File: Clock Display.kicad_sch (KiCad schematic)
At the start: 28 parts, among them U11 SA15-11SURKWA, U12 SA15-11SURKWA, U13 SA15-11SURKWA, U14 SA15-11SURKWA, U15 SA15-11SURKWA, U26 SN74LVC244A, U31 SN74LVC244A, U36 SN74LVC244A, U7 SA15-11SURKWA

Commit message: Restructuring
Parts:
- added C27: 1u, Capacitor_SMD:C_0402_1005Metric, symbol Device:C
- added R12, R13: 10R, symbol Device:R
- U11, U12, U13, U14, U15, U7: footprint (none) -> precision_clock:SA15-11SURKWA; Mouser (none) -> 604-SA15-11SURKWA
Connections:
- net GND: now also U31.11 (2A3), U31.13 (2A2), C27.2
- net K7: now also R12.2, R13.1; no longer U26.9 (2Y3)
- net VDIS: now also R13.2
- net DIS7: now reaches U26.11 (2A3)
- net DIS6: now reaches U26.13 (2A2)
- net DIS5: now reaches U26.15 (2A1)
- net DIS4: now reaches U26.17 (2A0)
- net DIS0: now reaches U26.2 (1A0)
- net DIS1: now reaches U26.4 (1A1)
- net DIS2: now reaches U26.6 (1A2)
- net DIS3: now reaches U26.8 (1A3)
- net DIS13: now reaches U31.15 (2A1)
- net DIS12: now reaches U31.17 (2A0)
- net DIS8: now reaches U31.2 (1A0)
- net DIS9: now reaches U31.4 (1A1)
- net DIS10: now reaches U31.6 (1A2)
- net DIS11: now reaches U31.8 (1A3)
- net VC renamed VCOL
- net VCOL: now also C27.1
- new net: R12.1, U26.9 (2Y3)
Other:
- note added: "Current Limiting resistors here needs to be reconsidered"
- note removed: "HHmmSSsss Character matrix drivers"
- moved on the sheet: C25, C26, C44, C45, C47, D16, D17, D18, D19, R45, R46, R47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

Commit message: Removal of Colon LEDs
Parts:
- removed D16, D17, D18, D19: LED, LED_THT:LED_D5.0mm, symbol Device:LED
- added D10, D7, D8, D9: LED, precision_clock:Lite On LTST-C190KxKT, symbol Device:LED
- C37: renamed from C27; footprint Capacitor_SMD:C_0402_1005Metric -> Capacitor_SMD:C_0603_1608Metric
- R16: renamed from R12; footprint (none) -> Resistor_SMD:R_0402_1005Metric
- R17: renamed from R13; footprint (none) -> Resistor_SMD:R_0402_1005Metric
- R28: renamed from R45; footprint Resistor_SMD:R_0603_1608Metric -> Resistor_SMD:R_0402_1005Metric
- R29: renamed from R46; footprint Resistor_SMD:R_0603_1608Metric -> Resistor_SMD:R_0402_1005Metric
- R30: renamed from R47; footprint Resistor_SMD:R_0603_1608Metric -> Resistor_SMD:R_0402_1005Metric
- R31: renamed from R48; footprint Resistor_SMD:R_0603_1608Metric -> Resistor_SMD:R_0402_1005Metric
- R32: renamed from R49; footprint Resistor_SMD:R_0603_1608Metric -> Resistor_SMD:R_0402_1005Metric
- R33: renamed from R50; footprint Resistor_SMD:R_0603_1608Metric -> Resistor_SMD:R_0402_1005Metric
- R34: renamed from R51; footprint Resistor_SMD:R_0603_1608Metric -> Resistor_SMD:R_0402_1005Metric
- R35: renamed from R52; footprint Resistor_SMD:R_0603_1608Metric -> Resistor_SMD:R_0402_1005Metric
- R36: renamed from R53; footprint Resistor_SMD:R_0603_1608Metric -> Resistor_SMD:R_0402_1005Metric
- R37: renamed from R54; footprint Resistor_SMD:R_0603_1608Metric -> Resistor_SMD:R_0402_1005Metric
- renumbered C25 to C27, C44 to C28, C26 to C33, C45 to C34, C47 to C38, U7 to U10, U26 to U11, U11 to U12, U12 to U13, U31 to U14, U13 to U15, U14 to U16, U36 to U17, U15 to U18
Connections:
- net COL0 is gone; now on net LED0: U17.2 (1A0)
- net COL1 is gone; now on net LED1: U17.4 (1A1)
- net COL2 is gone; now on net LED2: U17.6 (1A2)
- net COL3 is gone; now on net LED3: U17.8 (1A3)
- net GND: now also D10.1 (K), D7.1 (K), D8.1 (K), D9.1 (K)
- net LED0: no longer R34.1, U17.18 (1Y0)
- net LED1: no longer R35.1, U17.16 (1Y1)
- net LED2: no longer R36.1, U17.14 (1Y2)
- net LED3: no longer R37.1, U17.12 (1Y3)
- net at R37.2: now also D10.2 (A)
- net at R36.2: now also D9.2 (A)
- net at R35.2: now also D8.2 (A)
- net at R34.2: now also D7.2 (A)
- net VCOL renamed +3.3V
- new net: R35.1, U17.16 (1Y1)
- new net: R37.1, U17.12 (1Y3)
- new net: R36.1, U17.14 (1Y2)
- new net: R34.1, U17.18 (1Y0)
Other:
- note removed: "HH:mm separator"
- note removed: "mm:SS separator"
- moved on the sheet: C27, C28, C33, C34, C37, C38, R16, R17, R28, R29, R30, R31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

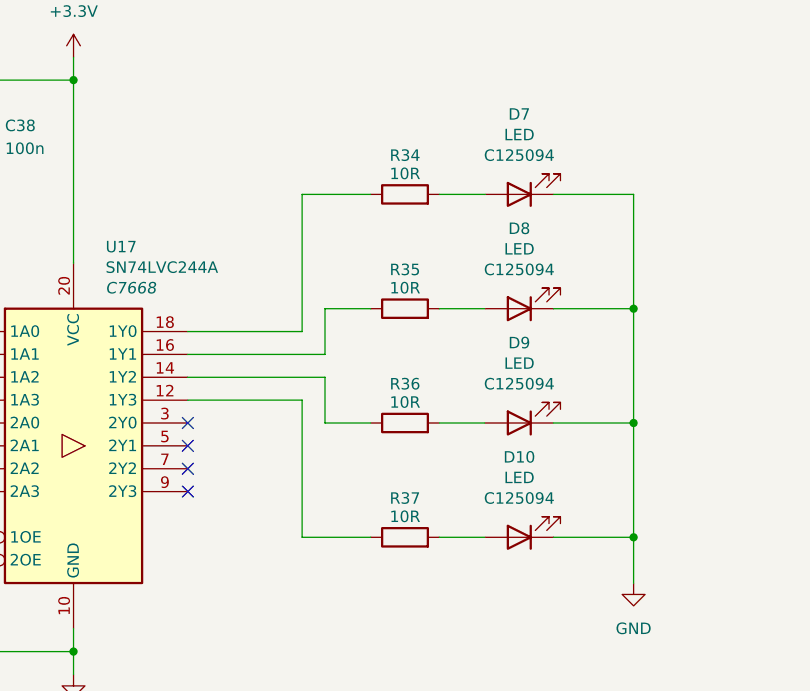
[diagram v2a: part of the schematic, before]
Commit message: buzzer and ambient light sensor added
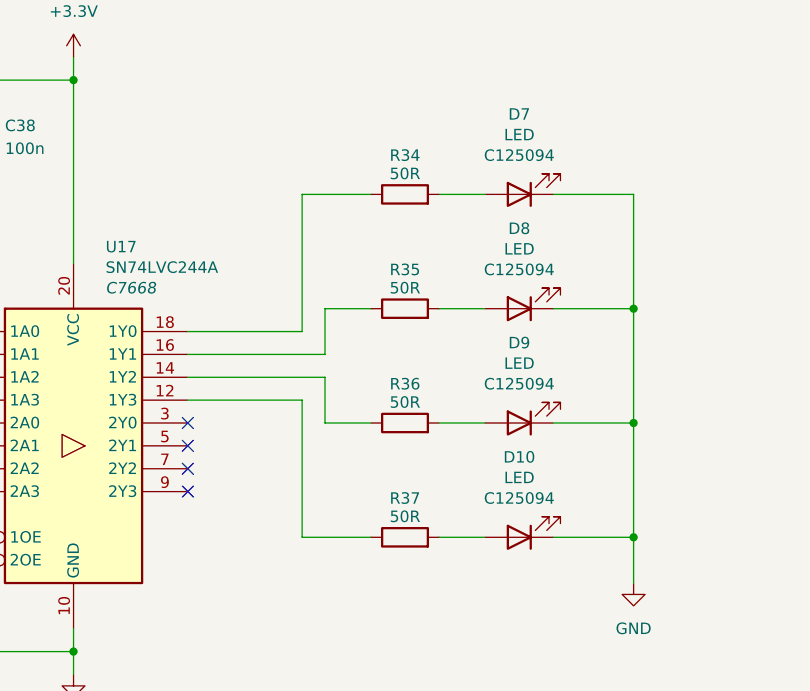
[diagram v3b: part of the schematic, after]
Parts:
- R34, R35, R36, R37: value 10R -> 50R
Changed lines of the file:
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@@
 			)
 		)
-		(property "Value" "10R"
+		(property "Value" "50R"
 			(at 341.63 175.514 90)
 			(effects
@@
 			)
 		)
-		(property "Value" "10R"
+		(property "Value" "50R"
 			(at 341.63 200.914 90)
 			(effects
@@
 			)
 		)
-		(property "Value" "10R"
+		(property "Value" "50R"
 			(at 341.63 188.214 90)
 			(effects
@@
 			)
 		)
-		(property "Value" "10R"
+		(property "Value" "50R"
 			(at 341.63 162.814 90)
 			(effects

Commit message: removal of sensors
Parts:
- R34, R35, R36, R37: value 50R -> 10R
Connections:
- net +3.3V renamed VLED
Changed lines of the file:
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@@
 			)
 		)
-		(property "Value" "50R"
+		(property "Value" "10R"
 			(at 341.63 175.514 90)
 			(effects
@@
 	)
 	(symbol
-		(lib_id "power:+3.3V")
-		(at 304.8 149.86 0)
-		(unit 1)
-		(exclude_from_sim no)
-		(in_bom yes)
-		(on_board yes)
-		(dnp no)
-		(fields_autoplaced yes)
-		(property "Reference" "#PWR095"
-			(at 304.8 153.67 0)
-			(effects
-				(font
-					(size 1.27 1.27)
-				)
-				(hide yes)
-			)
-		)
-		(property "Value" "+3.3V"
-			(at 304.8 144.78 0)
-			(effects
-				(font
-					(size 1.27 1.27)
-				)
-			)
-		)
-		(property "Footprint" ""
-			(at 304.8 149.86 0)
-			(effects
-				(font
-					(size 1.27 1.27)
-				)
-				(hide yes)
-			)
-		)
-		(property "Datasheet" ""
-			(at 304.8 149.86 0)
-			(effects
-				(font
-					(size 1.27 1.27)
-				)
-				(hide yes)
-			)
-		)
-		(property "Description" "Power symbol creates a global label with name \"+3.3V\""
-			(at 304.8 149.86 0)
-			(effects
-				(font
-					(size 1.27 1.27)
-				)
-				(hide yes)
-			)
-		)
-		(pin "1"
-		)
-		(instances
-			(project ""
-				(path "/c9a8ff63-a0d1-4125-9dd1-40fb53daf536/d3af2bc2-13e8-43c1-8a6d-735ddffde2e2"
-					(reference "#PWR095")
-					(unit 1)
-				)
-			)
-		)
-	)
-	(symbol
 		(lib_id "Device:R")
 		(at 219.71 175.26 90)
@@
 			)
 		)
-		(property "Value" "50R"
+		(property "Value" "10R"
 			(at 341.63 200.914 90)
 			(effects
@@
 			)
 		)
-		(property "Value" "50R"
+		(property "Value" "10R"
 			(at 341.63 188.214 90)
 			(effects
@@
 			)
 		)
-		(property "Value" "50R"
+		(property "Value" "10R"
 			(at 341.63 162.814 90)
 			(effects
@@
 					(unit 1)
 				)
+			)
+		)
+	)
+	(symbol
+		(lib_id "power:+3.3V")
+		(at 304.8 149.86 0)
+		(unit 1)
+		(exclude_from_sim no)
+		(in_bom yes)
+		(on_board yes)
+		(dnp no)
+		(fields_autoplaced yes)
+		(property "Reference" "#PWR017"
+			(at 304.8 153.67 0)
+			(effects
+				(font
+					(size 1.27 1.27)
+				)
+				(hide yes)
+			)
+		)
+		(property "Value" "VLED"
+			(at 304.8 144.78 0)
+			(effects
+				(font
+					(size 1.27 1.27)
+				)
+			)
+		)
+		(property "Footprint" ""
+			(at 304.8 149.86 0)
+			(effects
+				(font
+					(size 1.27 1.27)
+				)
+				(hide yes)
+			)
+		)
+		(property "Datasheet" ""
+			(at 304.8 149.86 0)
+			(effects
+				(font
+					(size 1.27 1.27)
+				)
+				(hide yes)
+			)
+		)
+		(property "Description" "Power symbol creates a global label with name \"+3.3V\""
+			(at 304.8 149.86 0)
+			(effects
+				(font
+					(size 1.27 1.27)
+				)
+				(hide yes)
+			)
+		)
+		(pin "1"
+		)
+		(instances
+			(project "Precision Clock"
+				(path "/c9a8ff63-a0d1-4125-9dd1-40fb53daf536/d3af2bc2-13e8-43c1-8a6d-735ddffde2e2"
+					(reference "#PWR017")
+					(unit 1)
+				)

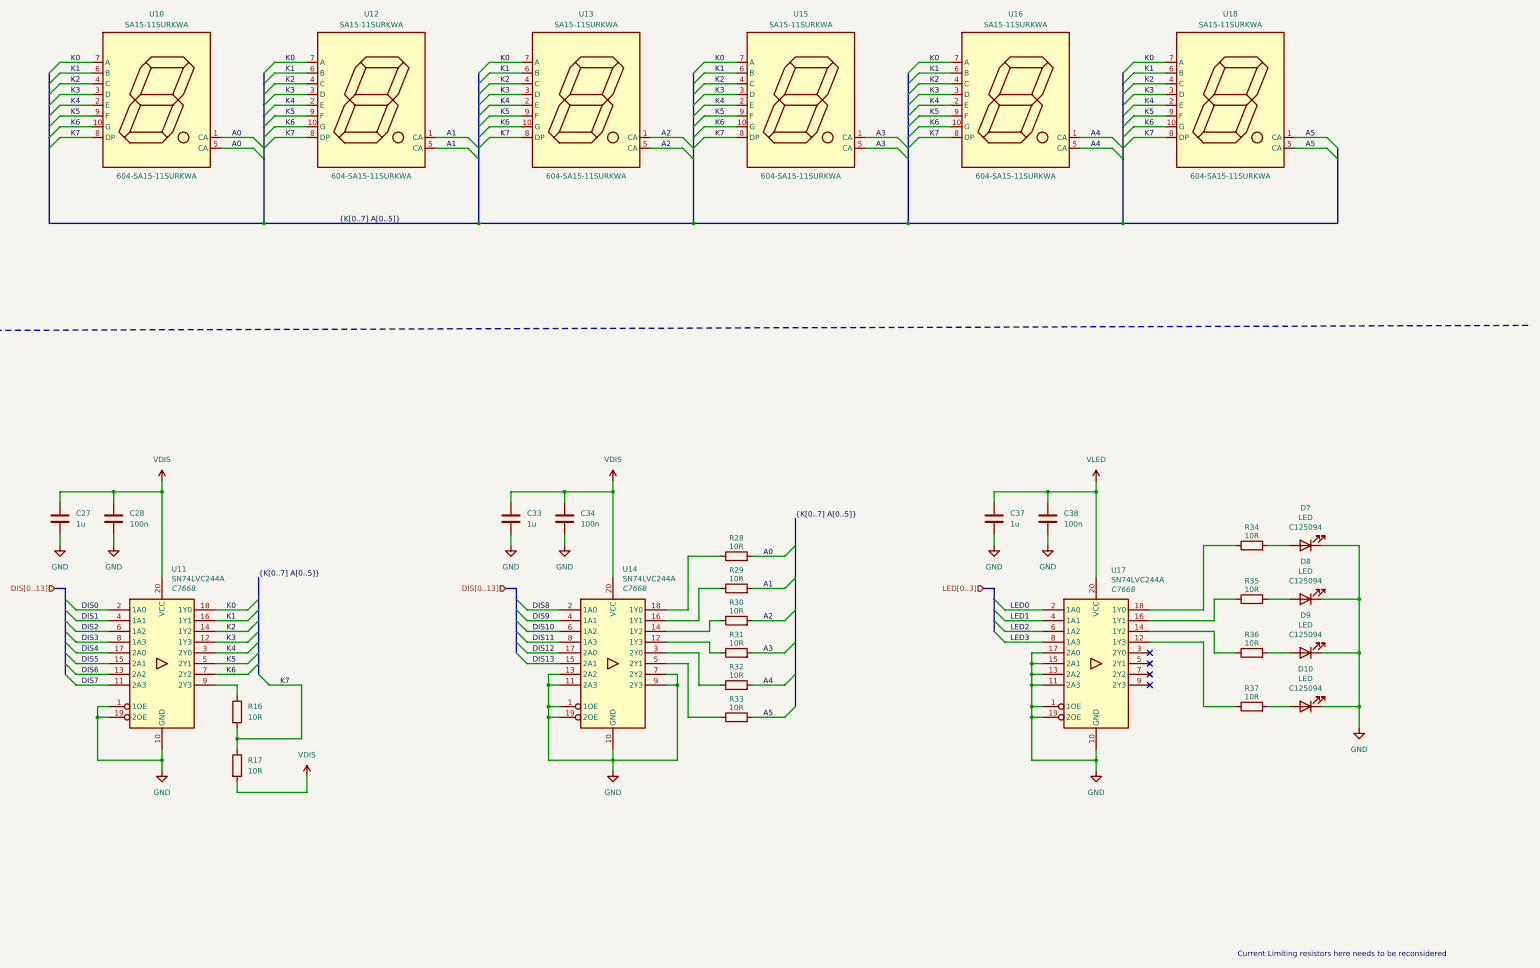
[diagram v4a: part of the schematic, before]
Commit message: addition of BME690
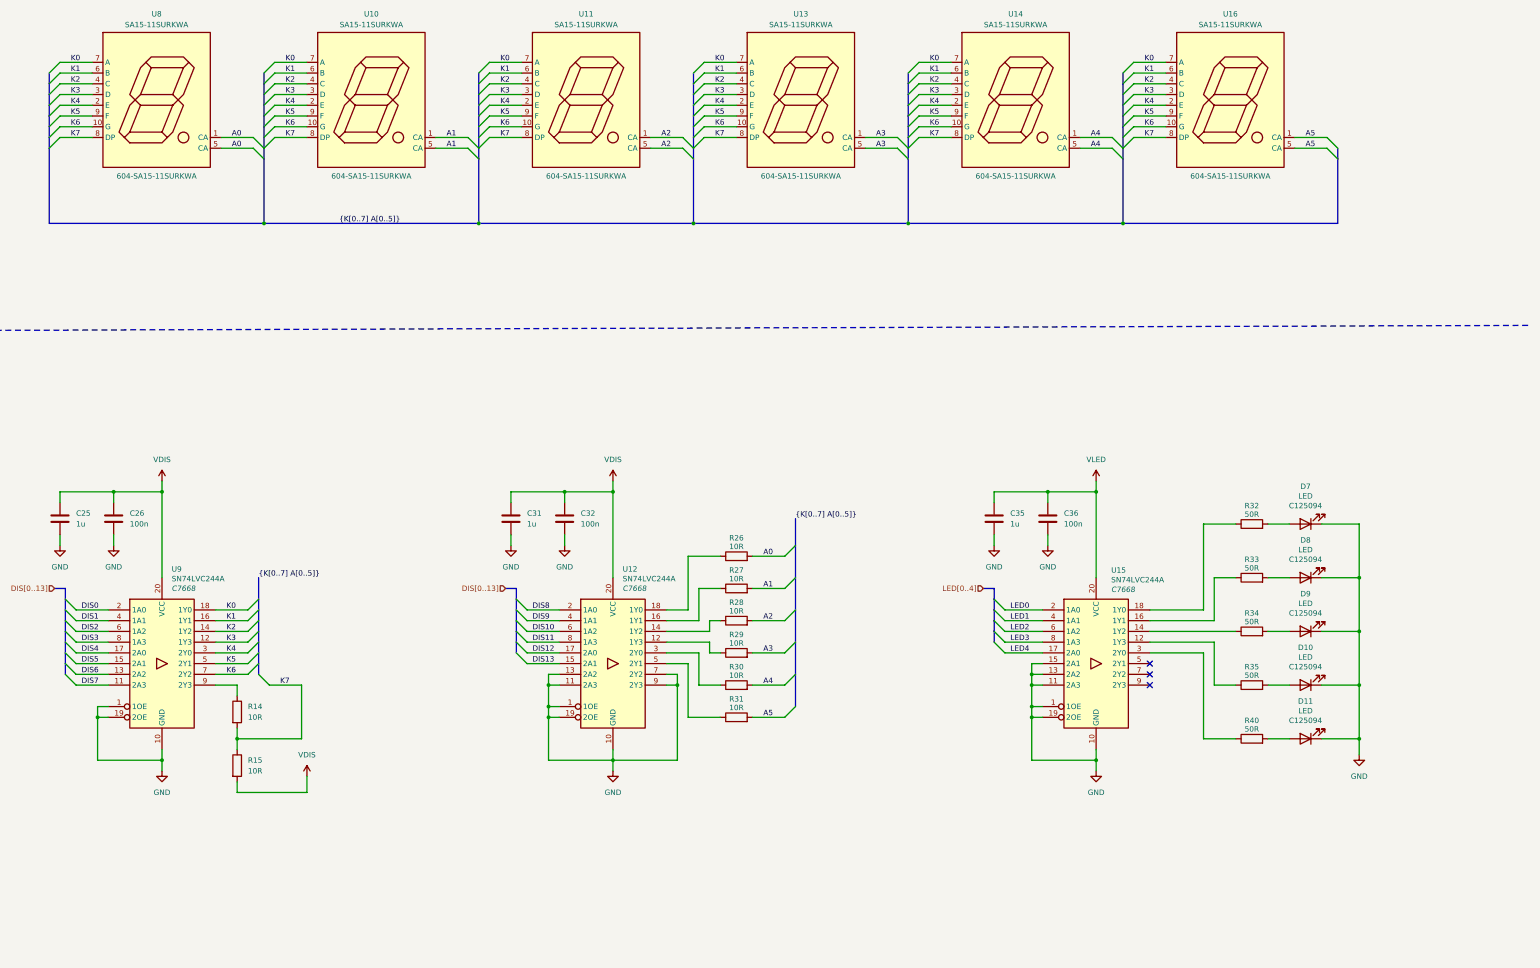
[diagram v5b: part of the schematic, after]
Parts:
- added D11: LED, precision_clock:Lite On LTST-C190KxKT, symbol Device:LED
- added R40: 50R, Resistor_SMD:R_0402_1005Metric, symbol Device:R
- R32: renamed from R34; value 10R -> 50R
- R33: renamed from R35; value 10R -> 50R
- R34: renamed from R36; value 10R -> 50R
- R35: renamed from R37; value 10R -> 50R
- renumbered C27 to C25, C28 to C26, C33 to C31, C34 to C32, C37 to C35, C38 to C36, R16 to R14, R17 to R15, R28 to R26, R29 to R27, R30 to R28, R31 to R29, R32 to R30, R33 to R31, U12 to U10, U13 to U11, U14 to U12, U15 to U13, U16 to U14, U17 to U15, U18 to U16, U10 to U8, U11 to U9
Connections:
- net GND: now also D11.1 (K); no longer U15.17 (2A0)
- net at U15.3 (2Y0): now also R40.1
- new net: D11.2 (A), R40.2
- new net LED4: U15.17 (2A0)
- no-connect marks 4 -> 3
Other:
- note removed: "Current Limiting resistors here needs to be reconsidered"
- moved on the sheet: D10, D7, D8, D9, R32, R33, R34, R35

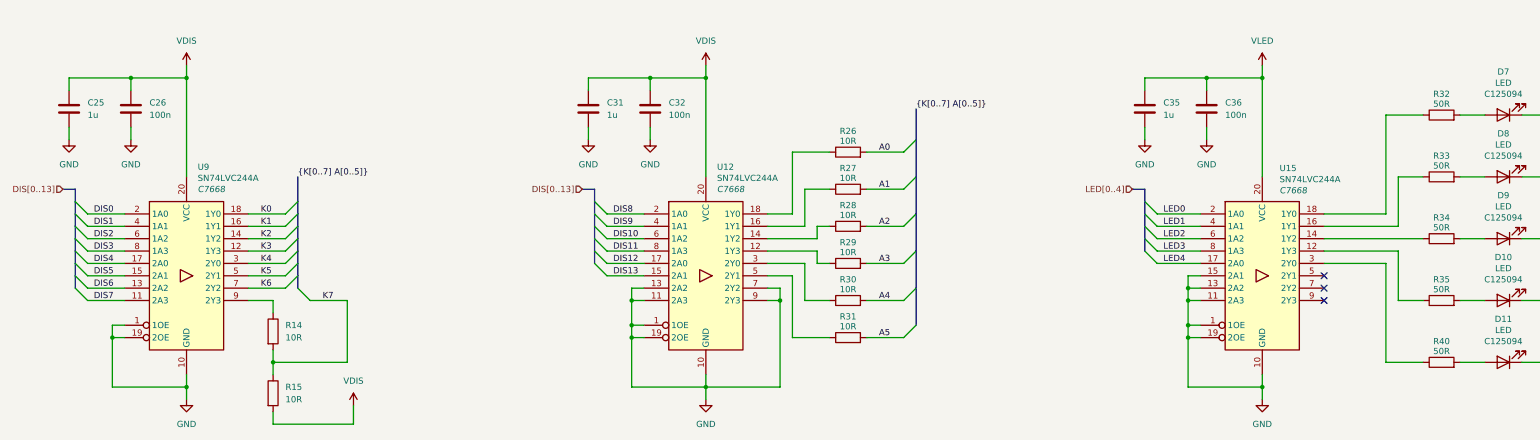
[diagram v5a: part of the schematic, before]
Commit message: Verification
- changed the piezo electric speaker.
- verified some schematics
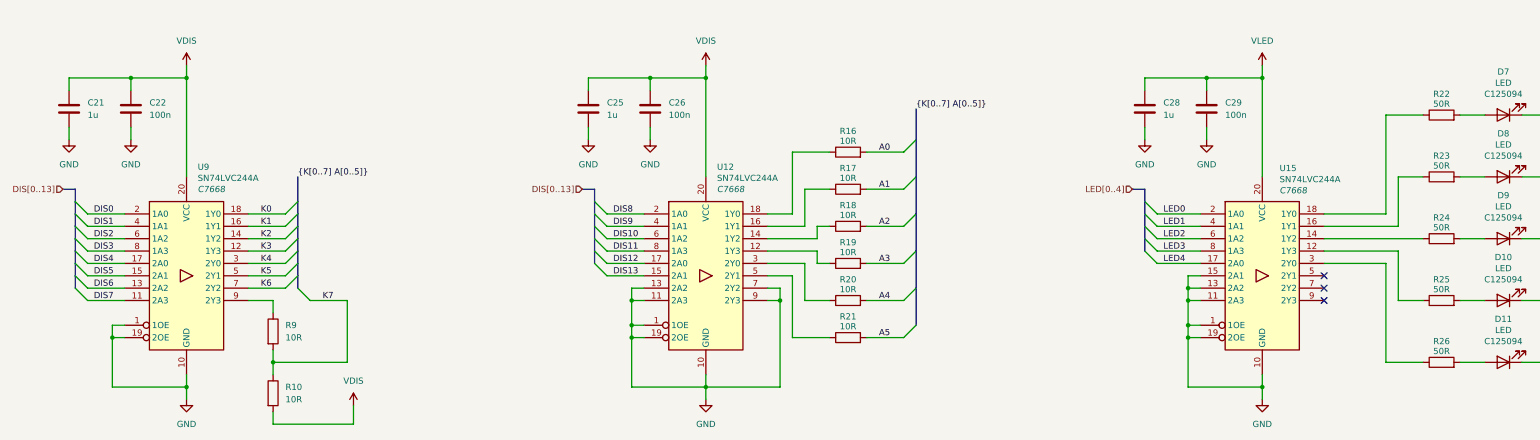
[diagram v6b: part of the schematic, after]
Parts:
- renumbered C25 to C21, C26 to C22, C31 to C25, C32 to C26, C35 to C28, C36 to C29, R15 to R10, R26 to R16, R27 to R17, R28 to R18, R29 to R19, R30 to R20, R31 to R21, R32 to R22, R33 to R23, R34 to R24, R35 to R25, R40 to R26, R14 to R9

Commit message: Power subsystem updated
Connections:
- net GND: no longer U12.7 (2Y2), U12.9 (2Y3)
- no-connect marks 3 -> 5
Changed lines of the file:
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@@
 	)
 	(junction
-		(at 205.74 198.12)
-		(diameter 0)
-		(color 0 0 0 0)
-	)
-	(junction
 		(at 311.15 88.9)
 		(diameter 0)
@@
 	)
 	(no_connect
+		(at 203.2 195.58)
+	)
+	(no_connect
 		(at 317.5 195.58)
 	)
@@
 		(at 317.5 198.12)
 	)
+	(no_connect
+		(at 203.2 198.12)
+	)
 	(bus_entry
 		(at 233.68 172.72)
@@
 	(wire
 		(pts
-			(xy 203.2 195.58) (xy 205.74 195.58)
-		)
-		(stroke
-			(width 0)
-			(type default)
-		)
-	)
-	(wire
-		(pts
 			(xy 212.09 53.34) (xy 219.71 53.34)
 		)
@@
 		)
 	)
-	(wire
-		(pts
-			(xy 203.2 198.12) (xy 205.74 198.12)
-		)
-		(stroke
-			(width 0)
-			(type default)
-		)
-	)
 	(bus
 		(pts
@@
 	(wire
 		(pts
-			(xy 205.74 198.12) (xy 205.74 215.9)
-		)
-		(stroke
-			(width 0)
-			(type default)
-		)
-	)
-	(wire
-		(pts
 			(xy 280.67 162.56) (xy 280.67 165.1)
 		)
@@
 	(wire
 		(pts
-			(xy 205.74 215.9) (xy 190.5 215.9)
-		)
-		(stroke
-			(width 0)
-			(type default)
-		)
-	)
-	(wire
-		(pts
 			(xy 161.29 53.34) (xy 168.91 53.34)
 		)
@@
 		)
 		(stroke
-			(width 0)
-			(type default)
-		)
-	)
-	(wire
-		(pts
-			(xy 205.74 195.58) (xy 205.74 198.12)
-		)
-		(stroke

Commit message: Verification
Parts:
- removed C28: 1u, Capacitor_SMD:C_0603_1608Metric, symbol Device:C
- removed C29: 100n, Capacitor_SMD:C_0402_1005Metric, symbol Device:C
- removed D10, D11, D7, D8, D9: LED, precision_clock:Lite On LTST-C190KxKT, symbol Device:LED
- removed R10: 10R, Resistor_SMD:R_0402_1005Metric, symbol Device:R
- removed R22, R23, R24, R25, R26: 50R, Resistor_SMD:R_0402_1005Metric, symbol Device:R
- removed U13, U16: SA15-11SURKWA, precision_clock:SA15-11SURKWA, symbol precision_clock:SA15-11SURKWA
- removed U15: SN74LVC244A, Package_SO:TSSOP-20_4.4x6.5mm_P0.65mm, symbol 74xx:74AHC244
- added U12, U15: SA15-11SURKWA, precision_clock:SA15-11SURKWA, symbol precision_clock:SA15-11SURKWA
- renumbered C21 to C24, C22 to C26, C26 to C27, R9 to R13, R16 to R15, R17 to R16, R18 to R17, R19 to R18, R20 to R19, R21 to R20, U8 to U10, U10 to U13, U9 to U8, U12 to U9
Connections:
- net A3: now also U14.1 (CA), U14.5 (CA)
- net A4: now also U12.1 (CA), U12.5 (CA); no longer U14.1 (CA), U14.5 (CA)
- net A5: now also U15.1 (CA), U15.5 (CA)
- net K0: now also U12.7 (A), U15.7 (A)
- net K1: now also U12.6 (B), U15.6 (B)
- net K2: now also U12.4 (C), U15.4 (C)
- net K3: now also U12.3 (D), U15.3 (D)
- net K4: now also U12.2 (E), U15.2 (E)
- net K5: now also U12.9 (F), U15.9 (F)
- net K6: now also U12.10 (G), U15.10 (G)
- net K7: now also U12.8 (DP), U15.8 (DP)
- no-connect marks 5 -> 2
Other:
- note added: "Display Segments"
- note added: "Driver 0"
- note added: "Driver 1"
- note added: "duty cycle of the DP should be half of that of segments"
- moved on the sheet: C24, C25, C26, C27, R13, R15, R16, R17, R18, R19, R20, U10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
